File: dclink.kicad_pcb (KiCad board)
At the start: 2 copper layers, 57.5 x 55.5 mm, 2 parts, among them U1 dcb-310

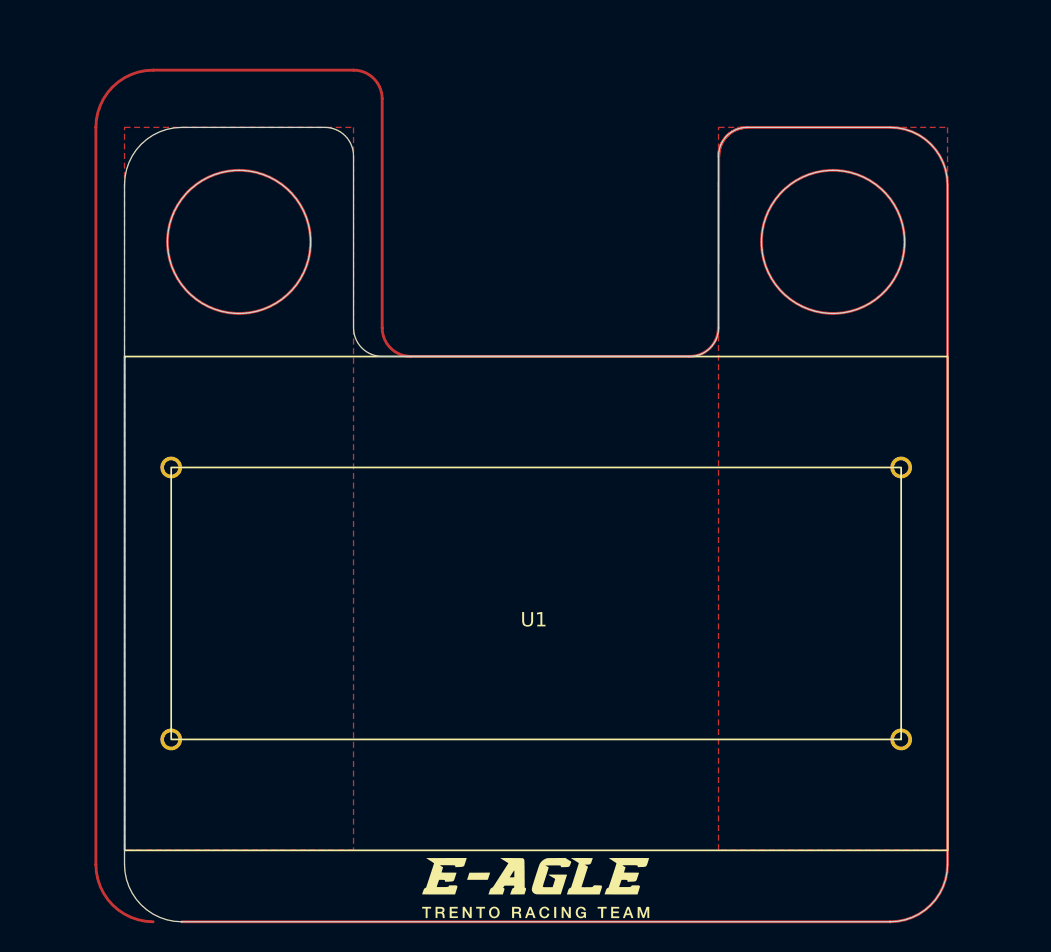
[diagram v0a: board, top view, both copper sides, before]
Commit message: new footprint, TODO: pad connections
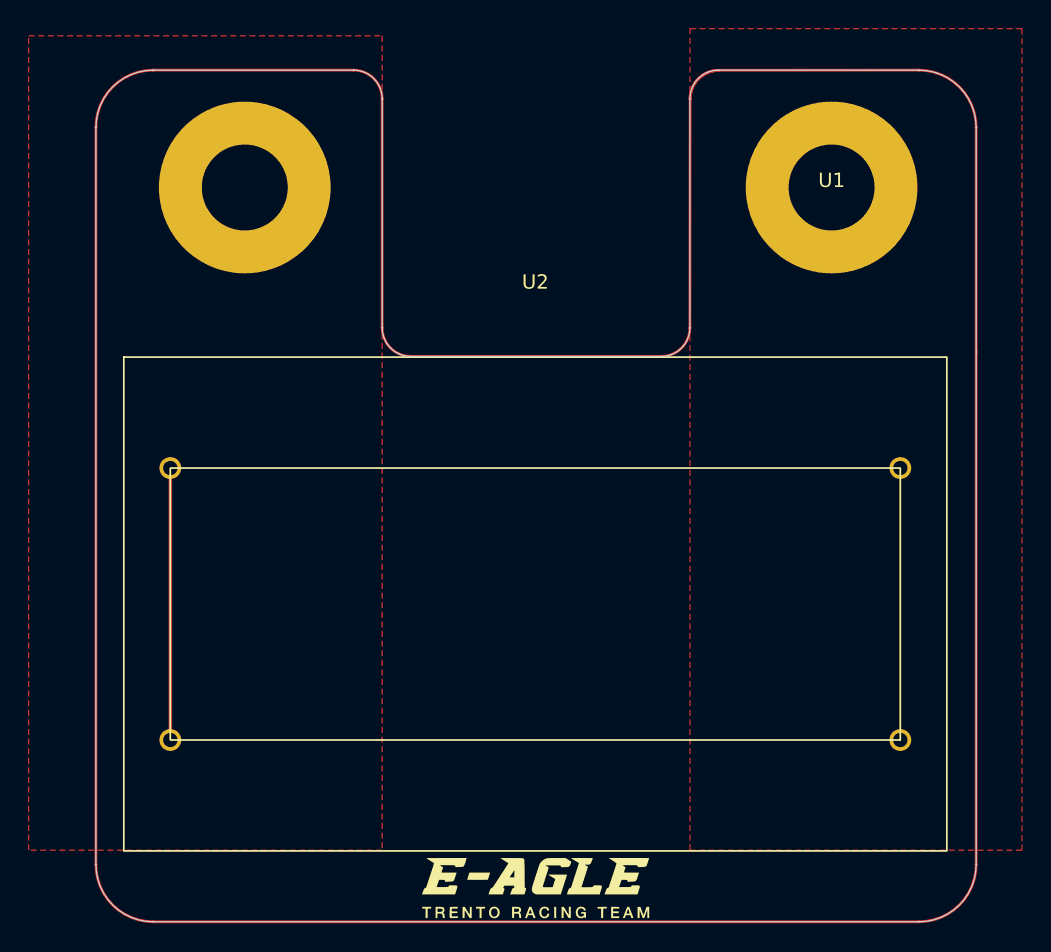
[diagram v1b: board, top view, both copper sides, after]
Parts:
- added U2: dcb-310, dcbk310:dcb-k310, F.Cu at (149.8, 102.3)
- U1: value dcb-310 -> mounting_holes; footprint dcbk310:dcb-k310 -> dcbk310:mounting_holes
- moved U1 28.4 mm to (170.5, 82.7)
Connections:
- U1 pad 1: unconnected-(U1-Pad1) -> (no net)
- U1 pad 2: unconnected-(U1-Pad2) -> (no net)
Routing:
- net Net-(U1-Pad)_1: track 0.00 -> 19.0 mm
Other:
- board size 57.5 x 55.5 mm -> 61.5 x 59.5 mm
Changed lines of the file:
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@@
   )
   (net 0 "")
-  (net 1 "unconnected-(U1-Pad1)")
-  (net 2 "unconnected-(U1-Pad2)")
-  (net 3 "unconnected-(U1-Pad3)")
-  (net 4 "unconnected-(U1-Pad4)")
+  (net 1 "Net-(U1-Pad)_1")
+  (net 2 "Net-(U1-Pad)")
   (footprint "LM393:logosenzascritta" (layer "F.Cu")
     (at 149.9 131.6)
@@
       ) (layer "F.SilkS") (width 0) (fill solid))
   )
-  (footprint "dcbk310:dcb-k310" (layer "F.Cu")
-    (at 149.86 102.26)
+  (footprint "dcbk310:mounting_holes" (layer "F.Cu")
+    (at 170.5 82.7)
     (property "Sheetfile" "dclink.kicad_sch")
     (property "Sheetname" "")
     (attr through_hole)
-    (fp_text reference "U1" (at -0.16 10.64 unlocked) (layer "F.SilkS")
+    (fp_text reference "U1" (at 0 -0.5 unlocked) (layer "F.SilkS")
       (effects (font (size 1 1) (thickness 0.15)))
     )
-    (fp_text value "dcb-310" (at -0.16 8.14 unlocked) (layer "F.Fab")
+    (fp_text value "mounting_holes" (at 0 1 unlocked) (layer "F.Fab")
       (effects (font (size 1 1) (thickness 0.15)))
     )
-    (fp_text user "${REFERENCE}" (at -0.16 10.64 unlocked) (layer "F.Fab")
+    (fp_text user "${REFERENCE}" (at 0 2.5 unlocked) (layer "F.Fab")
       (effects (font (size 1 1) (thickness 0.15)))
     )
+    (pad "1" thru_hole circle (at -41 0) (size 12 12) (drill 6) (layers *.Cu *.Mask)
+      (zone_connect 2))
+    (pad "2" thru_hole circle (at 0 0) (size 12 12) (drill 6) (layers *.Cu *.Mask)
+      (zone_connect 2))
+  )
+  (footprint "dcbk310:dcb-k310" (layer "F.Cu")
+    (at 149.8 102.3)
+    (property "Sheetfile" "dclink.kicad_sch")
+    (property "Sheetname" "")
+    (attr through_hole)
+    (fp_text reference "U2" (at 0 -13 unlocked) (layer "F.SilkS")
+      (effects (font (size 1 1) (thickness 0.15)))
+    )
+    (fp_text value "dcb-310" (at 0 -15.5 unlocked) (layer "F.Fab")
+      (effects (font (size 1 1) (thickness 0.15)))
+    )
+    (fp_text user "${REFERENCE}" (at 0 -13 unlocked) (layer "F.Fab")
+      (effects (font (size 1 1) (thickness 0.15)))
+    )
+    (fp_rect (start 25.5 19) (end -25.5 0) (layer "F.SilkS") (width 0.12) (fill none))
     (fp_rect (start -28.75 -7.75) (end 28.75 26.75) (layer "F.SilkS") (width 0.12) (fill none))
-    (fp_rect (start 25.5 19) (end -25.5 0) (layer "F.SilkS") (width 0.12) (fill none))
     (pad "1" thru_hole circle (at -25.5 0) (size 1.524 1.524) (drill 1) (layers *.Cu *.Mask)
-      (net 1 "unconnected-(U1-Pad1)") (pinfunction "SUP") (pintype "input") (zone_connect 2))
+      (net 1 "Net-(U1-Pad)_1") (pinfunction "SUP") (pintype "input") (zone_connect 2))
     (pad "2" thru_hole circle (at 25.5 0) (size 1.524 1.524) (drill 1) (layers *.Cu *.Mask)
-      (net 2 "unconnected-(U1-Pad2)") (pinfunction "GND") (pintype "output"))
+      (net 2 "Net-(U1-Pad)") (pinfunction "GND") (pintype "output"))
     (pad "3" thru_hole circle (at -25.5 19) (size 1.524 1.524) (drill 1) (layers *.Cu *.Mask)
-      (net 3 "unconnected-(U1-Pad3)") (pinfunction "SUP") (pintype "input"))
+      (net 1 "Net-(U1-Pad)_1") (pinfunction "SUP") (pintype "input"))
     (pad "4" thru_hole circle (at 25.5 19) (size 1.524 1.524) (drill 1) (layers *.Cu *.Mask)
-      (net 4 "unconnected-(U1-Pad4)") (pinfunction "GND") (pintype "output"))
+      (net 2 "Net-(U1-Pad)") (pinfunction "GND") (pintype "output"))
   )
-  (gr_line (start 174.6 78.5) (end 164.614214 78.5) (layer "F.Cu") (width 0.2))
-  (gr_arc (start 162.614214 80.5) (mid 163.2 79.085786) (end 164.614214 78.5) (layer "F.Cu") (width 0.2))
-  (gr_circle (center 129.1 86.5) (end 134.1 86.5) (layer "F.Cu") (width 0.2) (fill none))
-  (gr_arc (start 162.614214 80.5) (mid 163.2 79.085786) (end 164.614214 78.5) (layer "F.Cu") (width 0.2))
+  (gr_line (start 176.6 74.5) (end 162.614214 74.514214) (layer "F.Cu") (width 0.2))
+  (gr_arc (start 160.614214 76.514214) (mid 161.2 75.1) (end 162.614214 74.514214) (layer "F.Cu") (width 0.2))
+  (gr_arc (start 160.614214 76.514214) (mid 161.2 75.1) (end 162.614214 74.514214) (layer "F.Cu") (width 0.2))
   (gr_line (start 123.1 74.5) (end 137.1 74.5) (layer "F.Cu") (width 0.2))
-  (gr_arc (start 174.6 78.5) (mid 177.428427 79.671573) (end 178.6 82.5) (layer "F.Cu") (width 0.2))
-  (gr_line (start 162.614214 80.5) (end 162.585786 92.5) (layer "F.Cu") (width 0.2))
+  (gr_arc (start 176.6 74.5) (mid 179.428427 75.671573) (end 180.6 78.5) (layer "F.Cu") (width 0.2))
+  (gr_line (start 160.614214 76.514214) (end 160.6 92.5) (layer "F.Cu") (width 0.2))
   (gr_line (start 119.1 78.5) (end 119.1 130) (layer "F.Cu") (width 0.2))
-  (gr_line (start 178.6 94.5) (end 178.6 82.5) (layer "F.Cu") (width 0.2))
+  (gr_line (start 180.6 94.2) (end 180.6 78.5) (layer "F.Cu") (width 0.2))
   (gr_arc (start 123.1 134) (mid 120.271573 132.828427) (end 119.1 130) (layer "F.Cu") (width 0.2))
-  (gr_circle (center 170.6 86.5) (end 175.6 86.5) (layer "F.Cu") (width 0.2) (fill none))
   (gr_arc (start 119.1 78.5) (mid 120.271573 75.671573) (end 123.1 74.5) (layer "F.Cu") (width 0.2))
-  (gr_line (start 178.6 130) (end 178.6 94.5) (layer "F.Cu") (width 0.2))
-  (gr_arc (start 178.6 130) (mid 177.428427 132.828427) (end 174.6 134) (layer "F.Cu") (width 0.2))
+  (gr_line (start 180.6 130) (end 180.6 94.2) (layer "F.Cu") (width 0.2))
+  (gr_arc (start 180.6 130) (mid 179.428427 132.828427) (end 176.6 134) (layer "F.Cu") (width 0.2))
   (gr_line (start 139.1 76.5) (end 139.1 92.5) (layer "F.Cu") (width 0.2))
-  (gr_arc (start 162.585786 92.5) (mid 162 93.914214) (end 160.585786 94.5) (layer "F.Cu") (width 0.2))
-  (gr_line (start 160.585786 94.5) (end 141.1 94.5) (layer "F.Cu") (width 0.2))
+  (gr_arc (start 160.6 92.5) (mid 160.014214 93.914214) (end 158.6 94.5) (layer "F.Cu") (width 0.2))
+  (gr_line (start 158.6 94.5) (end 141.1 94.5) (layer "F.Cu") (width 0.2))
   (gr_arc (start 141.1 94.5) (mid 139.685786 93.914214) (end 139.1 92.5) (layer "F.Cu") (width 0.2))
   (gr_arc (start 137.1 74.5) (mid 138.514214 75.085786) (end 139.1 76.5) (layer "F.Cu") (width 0.2))
-  (gr_line (start 125.1 134) (end 174.6 134) (layer "F.Cu") (width 0.2))
-  (gr_line (start 135.1 78.5) (end 125.1 78.5) (layer "Edge.Cuts") (width 0.05))
-  (gr_line (start 125.1 134) (end 174.6 134) (layer "Edge.Cuts") (width 0.05))
-  (gr_arc (start 162.6 92.5) (mid 162.014214 93.914214) (end 160.6 94.5) (layer "Edge.Cuts") (width 0.05))
-  (gr_line (start 162.6 80.5) (end 162.6 92.5) (layer "Edge.Cuts") (width 0.05))
-  (gr_line (start 137.1 92.5) (end 137.1 80.5) (layer "Edge.Cuts") (width 0.05))
-  (gr_arc (start 135.1 78.5) (mid 136.514214 79.085786) (end 137.1 80.5) (layer "Edge.Cuts") (width 0.05))
-  (gr_line (start 160.6 94.5) (end 139.1 94.5) (layer "Edge.Cuts") (width 0.05))
-  (gr_arc (start 174.6 78.5) (mid 177.428427 79.671573) (end 178.6 82.5) (layer "Edge.Cuts") (width 0.05))
-  (gr_arc (start 178.6 130) (mid 177.428427 132.828427) (end 174.6 134) (layer "Edge.Cuts") (width 0.05))
-  (gr_arc (start 121.1 82.5) (mid 122.271573 79.671573) (end 125.1 78.5) (layer "Edge.Cuts") (width 0.05))
-  (gr_line (start 178.6 130) (end 178.6 82.5) (layer "Edge.Cuts") (width 0.05))
-  (gr_line (start 121.1 82.5) (end 121.1 130) (layer "Edge.Cuts") (width 0.05))
-  (gr_arc (start 139.1 94.5) (mid 137.685786 93.914214) (end 137.1 92.5) (layer "Edge.Cuts") (width 0.05))
-  (gr_arc (start 125.1 134) (mid 122.271573 132.828427) (end 121.1 130) (layer "Edge.Cuts") (width 0.05))
-  (gr_line (start 174.6 78.5) (end 164.6 78.5) (layer "Edge.Cuts") (width 0.05))
-  (gr_circle (center 129.1 86.5) (end 134.1 86.5) (layer "Edge.Cuts") (width 0.05) (fill none))
-  (gr_arc (start 162.6 80.5) (mid 163.185786 79.085786) (end 164.6 78.5) (layer "Edge.Cuts") (width 0.05))
-  (gr_circle (center 170.6 86.5) (end 175.6 86.5) (layer "Edge.Cuts") (width 0.05) (fill none))
+  (gr_line (start 123.1 134) (end 176.6 134) (layer "F.Cu") (width 0.2))
+  (gr_line (start 137.1 74.5) (end 123.1 74.5) (layer "Edge.Cuts") (width 0.05))
+  (gr_line (start 123.1 134) (end 176.6 134) (layer "Edge.Cuts") (width 0.05))
+  (gr_arc (start 160.6 92.5) (mid 160.014214 93.914214) (end 158.6 94.5) (layer "Edge.Cuts") (width 0.05))
+  (gr_line (start 160.6 76.5) (end 160.6 92.5) (layer "Edge.Cuts") (width 0.05))
+  (gr_line (start 139.1 92.5) (end 139.1 76.5) (layer "Edge.Cuts") (width 0.05))
+  (gr_arc (start 137.1 74.5) (mid 138.514214 75.085786) (end 139.1 76.5) (layer "Edge.Cuts") (width 0.05))
+  (gr_line (start 158.6 94.5) (end 141.1 94.5) (layer "Edge.Cuts") (width 0.05))
+  (gr_arc (start 176.6 74.5) (mid 179.428427 75.671573) (end 180.6 78.5) (layer "Edge.Cuts") (width 0.05))
+  (gr_arc (start 180.6 130) (mid 179.428427 132.828427) (end 176.6 134) (layer "Edge.Cuts") (width 0.05))
+  (gr_arc (start 119.1 78.5) (mid 120.271573 75.671573) (end 123.1 74.5) (layer "Edge.Cuts") (width 0.05))
+  (gr_line (start 180.6 130) (end 180.6 78.5) (layer "Edge.Cuts") (width 0.05))
+  (gr_line (start 119.1 78.5) (end 119.1 130) (layer "Edge.Cuts") (width 0.05))
+  (gr_arc (start 141.1 94.5) (mid 139.685786 93.914214) (end 139.1 92.5) (layer "Edge.Cuts") (width 0.05))
+  (gr_arc (start 123.1 134) (mid 120.271573 132.828427) (end 119.1 130) (layer "Edge.Cuts") (width 0.05))
+  (gr_line (start 176.6 74.5) (end 162.6 74.5) (layer "Edge.Cuts") (width 0.05))
+  (gr_arc (start 160.6 76.5) (mid 161.185786 75.085786) (end 162.6 74.5) (layer "Edge.Cuts") (width 0.05))
+  (segment (start 124.3 102.3) (end 124.3 121.3) (width 0.25) (layer "F.Cu") (net 1))
   (zone (net 0) (net_name "") (layer "F.Cu") (hatch edge 0.508)
     (connect_pads (clearance 0.508))
@@
     (polygon
       (pts
-        (xy 137.1 129)
-        (xy 121.1 129)
-        (xy 121.1 78.5)
-        (xy 137.1 78.5)
+        (xy 139.1 129)
+        (xy 114.4 129)
+        (xy 114.4 72.1)
+        (xy 139.1 72.1)
       )
     )
@@
     (polygon
       (pts
-        (xy 178.6 78.5)
-        (xy 178.6 129)
-        (xy 162.6 129)
-        (xy 162.6 78.5)
+        (xy 183.8 71.6)
+        (xy 183.8 129)
+        (xy 160.6 129)
+        (xy 160.6 71.6)
       )
     )

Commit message: TODO: add vias
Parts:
- moved U1 1.80 mm to (170.6, 84.5)
- moved U2 0.10 mm to (149.9, 102.3)
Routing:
- net Net-(U2-Pad1): track 19.0 -> 0.00 mm
- added copper zone on B.Cu, net (none)
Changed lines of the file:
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@@
   )
   (net 0 "")
-  (net 1 "Net-(U1-Pad)_1")
-  (net 2 "Net-(U1-Pad)")
+  (net 1 "Net-(U2-Pad1)")
+  (net 2 "Net-(U2-Pad2)")
   (footprint "LM393:logosenzascritta" (layer "F.Cu")
     (at 149.9 131.6)
@@
   )
   (footprint "dcbk310:mounting_holes" (layer "F.Cu")
-    (at 170.5 82.7)
+    (at 170.6 84.5)
     (property "Sheetfile" "dclink.kicad_sch")
     (property "Sheetname" "")
@@
   )
   (footprint "dcbk310:dcb-k310" (layer "F.Cu")
-    (at 149.8 102.3)
+    (at 149.9 102.3)
     (property "Sheetfile" "dclink.kicad_sch")
     (property "Sheetname" "")
@@
     (fp_rect (start -28.75 -7.75) (end 28.75 26.75) (layer "F.SilkS") (width 0.12) (fill none))
     (pad "1" thru_hole circle (at -25.5 0) (size 1.524 1.524) (drill 1) (layers *.Cu *.Mask)
-      (net 1 "Net-(U1-Pad)_1") (pinfunction "SUP") (pintype "input") (zone_connect 2))
+      (net 1 "Net-(U2-Pad1)") (pinfunction "SUP") (pintype "input") (zone_connect 2))
     (pad "2" thru_hole circle (at 25.5 0) (size 1.524 1.524) (drill 1) (layers *.Cu *.Mask)
-      (net 2 "Net-(U1-Pad)") (pinfunction "GND") (pintype "output"))
+      (net 2 "Net-(U2-Pad2)") (pinfunction "GND") (pintype "output") (zone_connect 2))
     (pad "3" thru_hole circle (at -25.5 19) (size 1.524 1.524) (drill 1) (layers *.Cu *.Mask)
-      (net 1 "Net-(U1-Pad)_1") (pinfunction "SUP") (pintype "input"))
+      (net 1 "Net-(U2-Pad1)") (pinfunction "SUP") (pintype "input") (zone_connect 2))
     (pad "4" thru_hole circle (at 25.5 19) (size 1.524 1.524) (drill 1) (layers *.Cu *.Mask)
-      (net 2 "Net-(U1-Pad)") (pinfunction "GND") (pintype "output"))
+      (net 2 "Net-(U2-Pad2)") (pinfunction "GND") (pintype "output") (zone_connect 2))
   )
   (gr_line (start 176.6 74.5) (end 162.614214 74.514214) (layer "F.Cu") (width 0.2))
@@
   (gr_line (start 176.6 74.5) (end 162.6 74.5) (layer "Edge.Cuts") (width 0.05))
   (gr_arc (start 160.6 76.5) (mid 161.185786 75.085786) (end 162.6 74.5) (layer "Edge.Cuts") (width 0.05))
-  (segment (start 124.3 102.3) (end 124.3 121.3) (width 0.25) (layer "F.Cu") (net 1))
-  (zone (net 0) (net_name "") (layer "F.Cu") (hatch edge 0.508)
-    (connect_pads (clearance 0.508))
-    (min_thickness 0.254) (filled_areas_thickness no)
-    (fill yes (thermal_gap 0.508) (thermal_bridge_width 0.508))
+  (zone (net 0) (net_name "") (layers F&B.Cu) (hatch edge 0.508)
+    (connect_pads yes (clearance 0))
+    (min_thickness 0.0254) (filled_areas_thickness no)
+    (fill yes (thermal_gap 0.0254) (thermal_bridge_width 0.0254))
     (polygon
       (pts
@@
     )
   )
-  (zone (net 0) (net_name "") (layer "F.Cu") (hatch edge 0.508)
-    (connect_pads (clearance 0.508))
-    (min_thickness 0.254) (filled_areas_thickness no)
-    (fill yes (thermal_gap 0.508) (thermal_bridge_width 0.508))
+  (zone (net 0) (net_name "") (layers F&B.Cu) (hatch edge 0.508)
+    (connect_pads no (clearance 0))
+    (min_thickness 0.0254) (filled_areas_thickness no)
+    (fill yes (thermal_gap 0.0254) (thermal_bridge_width 0.0254))
     (polygon
       (pts
